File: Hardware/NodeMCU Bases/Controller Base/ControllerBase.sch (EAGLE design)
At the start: 7 parts

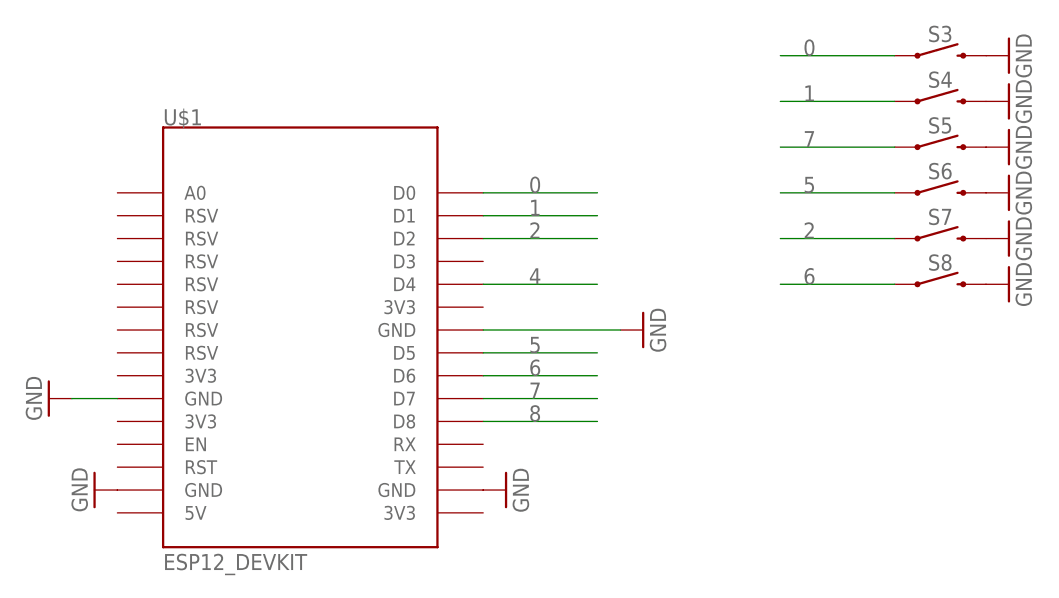
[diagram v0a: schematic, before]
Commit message: HEEP-949 updated from legacy cam for current Eagle Compatability. Also removed bName layer from bottom Silk
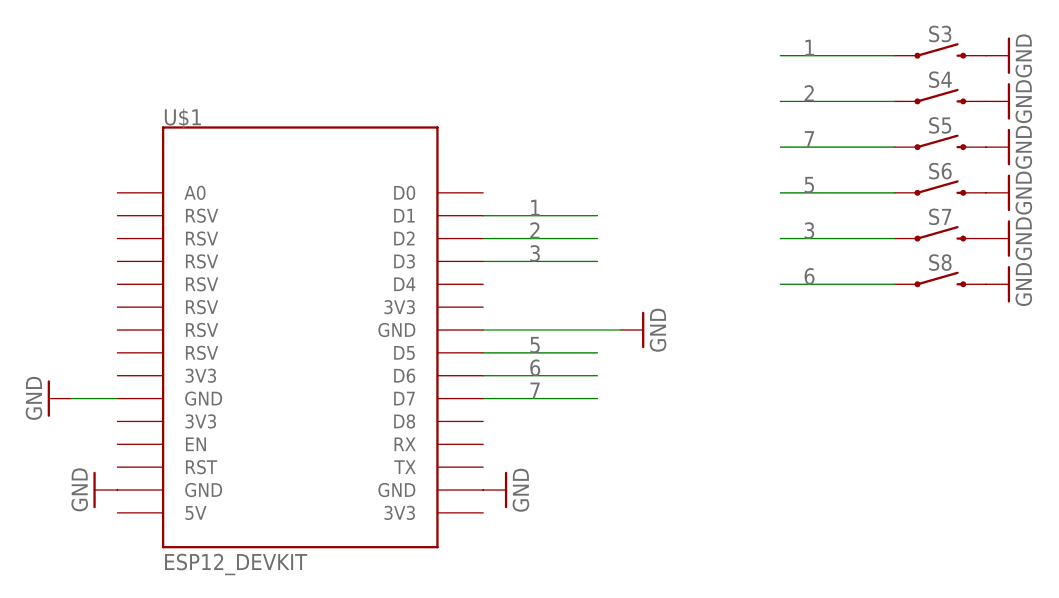
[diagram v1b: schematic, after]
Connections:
- removed net 0: S3.1, U$1.D0
- removed net 4: U$1.D4
- removed net 8: U$1.D8
- new net 3: S7.1, U$1.D3
- net 1: now also S3.1; no longer S4.1
- net 2: now also S4.1; no longer S7.1
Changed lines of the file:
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@@
 </segment>
 <segment>
-<wire x1="109.22" y1="68.58" x2="121.92" y2="68.58" width="0.1524" layer="91"/>
-<pinref part="S4" gate="G$1" pin="1"/>
-<label x="111.76" y="68.58" size="1.778" layer="95"/>
+<wire x1="109.22" y1="73.66" x2="121.92" y2="73.66" width="0.1524" layer="91"/>
+<pinref part="S3" gate="G$1" pin="1"/>
+<label x="111.76" y="73.66" size="1.778" layer="95"/>
 </segment>
 </net>
@@
 </segment>
 <segment>
-<wire x1="109.22" y1="53.34" x2="121.92" y2="53.34" width="0.1524" layer="91"/>
-<pinref part="S7" gate="G$1" pin="1"/>
-<label x="111.76" y="53.34" size="1.778" layer="95"/>
-</segment>
-</net>
-<net name="4" class="0">
-<segment>
-<wire x1="76.2" y1="48.26" x2="88.9" y2="48.26" width="0.1524" layer="91"/>
-<pinref part="U$1" gate="G$1" pin="D4"/>
-<label x="81.28" y="48.26" size="1.778" layer="95"/>
+<wire x1="109.22" y1="68.58" x2="121.92" y2="68.58" width="0.1524" layer="91"/>
+<pinref part="S4" gate="G$1" pin="1"/>
+<label x="111.76" y="68.58" size="1.778" layer="95"/>
 </segment>
 </net>
@@
 </segment>
 </net>
-<net name="0" class="0">
+<net name="3" class="0">
 <segment>
-<wire x1="76.2" y1="58.42" x2="88.9" y2="58.42" width="0.1524" layer="91"/>
-<pinref part="U$1" gate="G$1" pin="D0"/>
-<label x="81.28" y="58.42" size="1.778" layer="95"/>
+<pinref part="U$1" gate="G$1" pin="D3"/>
+<wire x1="76.2" y1="50.8" x2="88.9" y2="50.8" width="0.1524" layer="91"/>
+<label x="81.28" y="50.8" size="1.778" layer="95"/>
 </segment>
 <segment>
-<wire x1="109.22" y1="73.66" x2="121.92" y2="73.66" width="0.1524" layer="91"/>
-<pinref part="S3" gate="G$1" pin="1"/>
-<label x="111.76" y="73.66" size="1.778" layer="95"/>
+<wire x1="109.22" y1="53.34" x2="121.92" y2="53.34" width="0.1524" layer="91"/>
+<pinref part="S7" gate="G$1" pin="1"/>
+<label x="111.76" y="53.34" size="1.778" layer="95"/>
 </segment>
 </net>
-<net name="8" class="0">
-<segment>
-<pinref part="U$1" gate="G$1" pin="D8"/>
-<wire x1="76.2" y1="33.02" x2="88.9" y2="33.02" width="0.1524" layer="91"/>
-<label x="81.28" y="33.02" size="1.778" layer="95"/>
-</segment>
-</net>
